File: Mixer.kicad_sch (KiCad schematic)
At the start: 25 parts, among them J39 Noise Out, SW10 SW_SPDT, SW9 SW_SPDT, U11 TL071

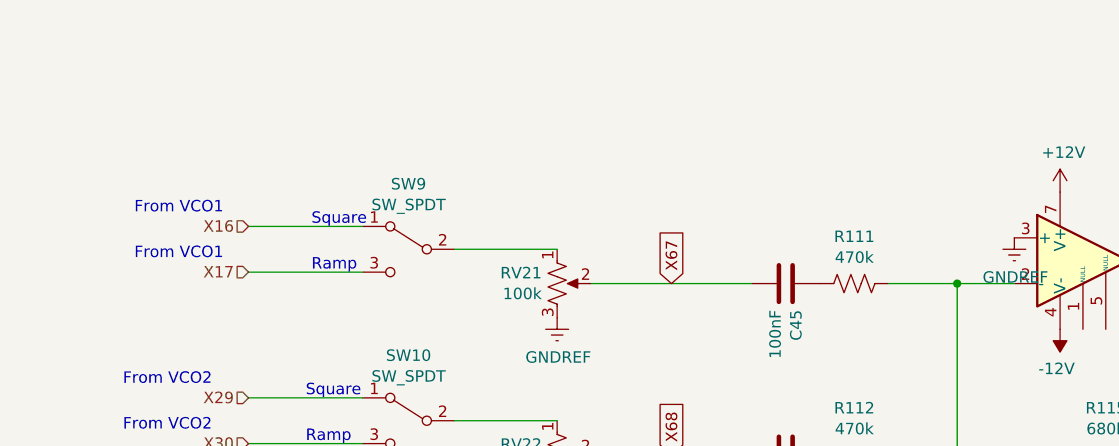
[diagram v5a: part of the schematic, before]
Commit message: lots of routes, added vco3, lfo2.
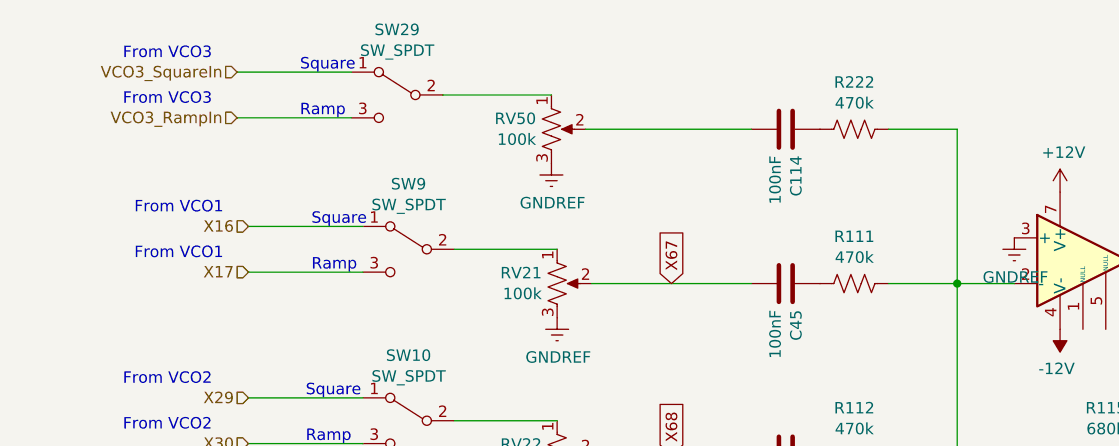
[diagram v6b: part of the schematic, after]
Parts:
- added C114: 100nF, Capacitor_SMD:C_0603_1608Metric, symbol Device:C
- added R222: 470k, Resistor_SMD:R_0603_1608Metric, symbol Device:R_US
- added RV50: 100k, Potentiometer_THT:Potentiometer_Alps_RK09K_Single_Vertical, symbol SynthProj-rescue:R_POT_US-Device
- added SW29: SW_SPDT, SynthProjConnectors:SMTS-102, symbol Switch:SW_SPDT
- J39: footprint SynthProjConnectors:PJ-301 -> SynthProjConnectors:PJ-301-BM
- SW10, SW9: footprint SynthProjConnectors:MTS-103-A01-T0 -> SynthProjConnectors:SMTS-102
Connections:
- net GNDREF: now also RV50.3
- net at R111.1, R112.1, R113.1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: now also R222.1
- new net: RV50.1, SW29.2 (B)
- new net: C114.1, R222.2
- new net: C114.2, RV50.2
- new net VCO3_RampIn: SW29.3 (C)
- new net VCO3_SquareIn: SW29.1 (A)
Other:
- note added: "From VCO3"
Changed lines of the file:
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@@
+    (stroke (width 0) (type default))
+  )
+  (wire (pts (xy 105.41 51.435) (xy 92.71 51.435))
     (stroke (width 0) (type default))
   )
@@
     (stroke (width 0) (type default))
   )
+  (wire (pts (xy 172.72 52.705) (xy 172.72 69.85))
+    (stroke (width 0) (type default))
+  )
   (wire (pts (xy 86.36 148.59) (xy 92.71 148.59))
     (stroke (width 0) (type default))
@@
     (stroke (width 0) (type default))
   )
+  (wire (pts (xy 105.41 46.355) (xy 92.71 46.355))
+    (stroke (width 0) (type default))
+  )
   (wire (pts (xy 132.08 69.85) (xy 149.86 69.85))
     (stroke (width 0) (type default))
@@
     (stroke (width 0) (type default))
   )
+  (wire (pts (xy 131.445 52.705) (xy 149.86 52.705))
+    (stroke (width 0) (type default))
+  )
+  (wire (pts (xy 115.57 48.895) (xy 127.635 48.895))
+    (stroke (width 0) (type default))
+  )
   (wire (pts (xy 201.93 88.9) (xy 201.93 67.31))
     (stroke (width 0) (type default))
@@
     (stroke (width 0) (type default))
   )
+  (wire (pts (xy 165.1 52.705) (xy 172.72 52.705))
+    (stroke (width 0) (type default))
+  )
   (wire (pts (xy 132.08 109.22) (xy 149.86 109.22))
     (stroke (width 0) (type default))
@@
     (effects (font (size 1.27 1.27)) (justify left bottom))
   )
+  (text "From VCO3" (at 80.01 50.165 0)
+    (effects (font (size 1.27 1.27)) (justify left bottom))
+  )
+  (text "Ramp" (at 99.695 51.435 0)
+    (effects (font (size 1.27 1.27)) (justify left bottom))
+  )
+  (text "Square" (at 99.695 46.355 0)
+    (effects (font (size 1.27 1.27)) (justify left bottom))
+  )
   (text "Ramp" (at 100.965 68.58 0)
+    (effects (font (size 1.27 1.27)) (justify left bottom))
+  )
+  (text "From VCO3" (at 80.01 45.085 0)
     (effects (font (size 1.27 1.27)) (justify left bottom))
   )
@@
     (effects (font (size 1.27 1.27)) (justify left))
   )
+  (hierarchical_label "VCO3_SquareIn" (shape input) (at 92.71 46.355 180) (fields_autoplaced)
+    (effects (font (size 1.27 1.27)) (justify right))
+  )
+  (hierarchical_label "VCO3_RampIn" (shape input) (at 92.71 51.435 180) (fields_autoplaced)
+    (effects (font (size 1.27 1.27)) (justify right))
+  )
   (hierarchical_label "X16" (shape input) (at 93.98 63.5 180) (fields_autoplaced)
     (effects (font (size 1.27 1.27)) (justify right))
@@
       (effects (font (size 1.27 1.27)))
     )
-    (property "Footprint" "SynthProjConnectors:MTS-103-A01-T0" (at 111.76 66.04 0)
+    (property "Footprint" "SynthProjConnectors:SMTS-102" (at 111.76 66.04 0)
       (effects (font (size 1.27 1.27)) hide)
     )
@@
       (effects (font (size 1.27 1.27)))
     )
-    (property "Footprint" "SynthProjConnectors:MTS-103-A01-T0" (at 111.76 85.09 0)
+    (property "Footprint" "SynthProjConnectors:SMTS-102" (at 111.76 85.09 0)
       (effects (font (size 1.27 1.27)) hide)
     )
@@
       (effects (font (size 1.27 1.27)))
     )
-    (property "Footprint" "SynthProjConnectors:PJ-301" (at 102.87 99.06 0)
+    (property "Footprint" "SynthProjConnectors:PJ-301-BM" (at 102.87 99.06 0)
       (effects (font (size 1.27 1.27)) hide)
     )
@@
     )
   )
+  (symbol (lib_id "Switch:SW_SPDT") (at 110.49 48.895 0) (mirror y) (unit 1)
+    (in_bom yes) (on_board yes) (dnp no)
+    (property "Reference" "SW29" (at 110.49 41.656 0)
+      (effects (font (size 1.27 1.27)))
+    )
+    (property "Value" "SW_SPDT" (at 110.49 43.9674 0)
+      (effects (font (size 1.27 1.27)))
+    )
+    (property "Footprint" "SynthProjConnectors:SMTS-102" (at 110.49 48.895 0)
+      (effects (font (size 1.27 1.27)) hide)
+    )
+    (property "Datasheet" "~" (at 110.49 48.895 0)
+      (effects (font (size 1.27 1.27)) hide)
+    )
+    (pin "1")
+    (pin "2")
+    (pin "3")
+    (instances
+      (project "SynthProj"
+        (path "/9021c97e-351f-4ed9-b393-50257df6a463/00000000-0000-0000-0000-00006611e0f5"
+          (reference "SW29") (unit 1)
+        )
+      )
+    )
+  )
+  (symbol (lib_id "Device:C") (at 153.67 52.705 270) (unit 1)
+    (in_bom yes) (on_board yes) (dnp no)
+    (property "Reference" "C114" (at 154.8384 55.626 0)
+      (effects (font (size 1.27 1.27)) (justify left))
+    )
+    (property "Value" "100nF" (at 152.527 55.626 0)
+      (effects (font (size 1.27 1.27)) (justify left))
+    )
+    (property "Footprint" "Capacitor_SMD:C_0603_1608Metric" (at 149.86 53.6702 0)
+      (effects (font (size 1.27 1.27)) hide)
+    )
+    (property "Datasheet" "~" (at 153.67 52.705 0)
+      (effects (font (size 1.27 1.27)) hide)
+    )
+    (pin "2")
+    (pin "1")
+    (instances
+      (project "SynthProj"
+        (path "/9021c97e-351f-4ed9-b393-50257df6a463/00000000-0000-0000-0000-00006611e0f5"
+          (reference "C114") (unit 1)
+        )
+        (path "/9021c97e-351f-4ed9-b393-50257df6a463/00000000-0000-0000-0000-0000659a4e2e"
+          (reference "C?") (unit 1)
+        )
+      )
+    )
+  )
+  (symbol (lib_id "SynthProj-rescue:R_POT_US-Device") (at 127.635 52.705 0) (unit 1)
+    (in_bom yes) (on_board yes) (dnp no)
+    (property "Reference" "RV50" (at 125.9332 51.5366 0)
+      (effects (font (size 1.27 1.27)) (justify right))
+    )
+    (property "Value" "100k" (at 125.9332 53.848 0)
+      (effects (font (size 1.27 1.27)) (justify right))
+    )
+    (property "Footprint" "Potentiometer_THT:Potentiometer_Alps_RK09K_Single_Vertical" (at 127.635 52.705 0)
+      (effects (font (size 1.27 1.27)) hide)
+    )
+    (property "Datasheet" "~" (at 127.635 52.705 0)
+      (effects (font (size 1.27 1.27)) hide)
+    )
+    (pin "3")
+    (pin "2")
+    (pin "1")
+    (instances
+      (project "SynthProj"
+        (path "/9021c97e-351f-4ed9-b393-50257df6a463/00000000-0000-0000-0000-00006611e0f5"
+          (reference "RV50") (unit 1)
+        )
+        (path "/9021c97e-351f-4ed9-b393-50257df6a463/00000000-0000-0000-0000-0000659a4e2e"
+          (reference "RV?") (unit 1)
+        )
+        (path "/9021c97e-351f-4ed9-b393-50257df6a463"
+          (reference "RV?") (unit 1)
+        )
+      )
+    )
+  )
   (symbol (lib_id "Device:C") (at 154.305 146.05 270) (unit 1)
     (in_bom yes) (on_board yes) (dnp no)
@@
         )
         (path "/9021c97e-351f-4ed9-b393-50257df6a463/00000000-0000-0000-0000-0000659a4e2e"
+          (reference "R?") (unit 1)
+        )
+      )
+    )
+  )
+  (symbol (lib_id "power:GNDREF") (at 127.635 56.515 0) (unit 1)
+    (in_bom yes) (on_board yes) (dnp no)
+    (property "Reference" "#PWR0255" (at 127.635 62.865 0)
+      (effects (font (size 1.27 1.27)) hide)
+    )
+    (property "Value" "GNDREF" (at 127.762 60.9092 0)
+      (effects (font (size 1.27 1.27)))
+    )
+    (property "Footprint" "" (at 127.635 56.515 0)
+      (effects (font (size 1.27 1.27)) hide)
+    )
+    (property "Datasheet" "" (at 127.635 56.515 0)
+      (effects (font (size 1.27 1.27)) hide)
+    )
+    (pin "1")
+    (instances
+      (project "SynthProj"
+        (path "/9021c97e-351f-4ed9-b393-50257df6a463/00000000-0000-0000-0000-00006611e0f5"
+          (reference "#PWR0255") (unit 1)
+        )
+      )
+    )
+  )
+  (symbol (lib_id "Device:R_US") (at 161.29 52.705 270) (unit 1)
+    (in_bom yes) (on_board yes) (dnp no)
+    (property "Reference" "R222" (at 161.29 47.498 90)
+      (effects (font (size 1.27 1.27)))
+    )
+    (property "Value" "470k" (at 161.29 49.8094 90)
+      (effects (font (size 1.27 1.27)))
+    )
+    (property "Footprint" "Resistor_SMD:R_0603_1608Metric" (at 161.036 53.721 90)
+      (effects (font (size 1.27 1.27)) hide)
+    )
+    (property "Datasheet" "~" (at 161.29 52.705 0)
+      (effects (font (size 1.27 1.27)) hide)
+    )
+    (pin "2")
+    (pin "1")
+    (instances
+      (project "SynthProj"
+        (path "/9021c97e-351f-4ed9-b393-50257df6a463/00000000-0000-0000-0000-00006611e0f5"
+          (reference "R222") (unit 1)
+        )
+        (path "/9021c97e-351f-4ed9-b393-50257df6a463/00000000-0000-0000-0000-0000659a4e2e"

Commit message: more and more and more and more and more routing
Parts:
- removed C39, C40: 4.7uF, Capacitor_SMD:C_0805_2012Metric, symbol Device:C
- removed C43, C44: 47nF, Capacitor_SMD:C_0603_1608Metric, symbol Device:C
- added C115, C116: 1uF, Capacitor_SMD:C_0805_2012Metric, symbol Device:C
- added R244, R245: 10k, Resistor_SMD:R_0603_1608Metric, symbol Device:R_US
- added RV42, RV52: 100k, Potentiometer_THT:Potentiometer_Alps_RK09K_Single_Vertical, symbol SynthProj-rescue:R_POT_US-Device
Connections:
- net GNDREF: now also RV42.3, RV52.3
- net at R111.1, R112.1, R113.1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: now also R244.1, R245.1
- net Mixer_ExtIn renamed Mixer_ExtIn1
- new net: C116.1, R245.2
- new net: C115.1, R244.2
- new net: C115.2, RV42.2
- new net: C116.2, RV52.2
- new net Mixer_ExtIn2: RV42.1
- new net Mixer_ExtIn3: RV52.1
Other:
- moved on the sheet: C41, C42, C93, R176

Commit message: created manufacturing files
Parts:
- R111, R112, R176, R222: value 470k -> 200k
- R114, R244, R245: value 10k -> 200k
- RV21, RV22, RV23, RV24, RV42, RV50, RV52: value 100k -> 50k
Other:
- note added: "Audio taper potentiometers for mixer inputs"
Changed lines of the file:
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@@
+    (effects (font (size 1.27 1.27)) (justify left bottom))
+  )
+  (text "Audio taper potentiometers for mixer inputs" (at 113.665 48.26 0)
     (effects (font (size 1.27 1.27)) (justify left bottom))
   )
@@
       (effects (font (size 1.27 1.27)) (justify right))
     )
-    (property "Value" "100k" (at 126.5682 70.993 0)
+    (property "Value" "50k" (at 126.5682 70.993 0)
       (effects (font (size 1.27 1.27)) (justify right))
     )
@@
       (effects (font (size 1.27 1.27)))
     )
-    (property "Value" "470k" (at 161.29 66.9544 90)
+    (property "Value" "200k" (at 161.29 66.9544 90)
       (effects (font (size 1.27 1.27)))
     )
@@
       (effects (font (size 1.27 1.27)))
     )
-    (property "Value" "470k" (at 161.29 86.0044 90)
+    (property "Value" "200k" (at 161.29 86.0044 90)
       (effects (font (size 1.27 1.27)))
     )
@@
       (effects (font (size 1.27 1.27)))
     )
-    (property "Value" "10k" (at 161.29 125.3744 90)
+    (property "Value" "200k" (at 161.29 125.3744 90)
       (effects (font (size 1.27 1.27)))
     )
@@
       (effects (font (size 1.27 1.27)) (justify right))
     )
-    (property "Value" "100k" (at 126.5682 90.043 0)
+    (property "Value" "50k" (at 126.5682 90.043 0)
       (effects (font (size 1.27 1.27)) (justify right))
     )
@@
       (effects (font (size 1.27 1.27)) (justify right))
     )
-    (property "Value" "100k" (at 126.5682 110.363 0)
+    (property "Value" "50k" (at 126.5682 110.363 0)
       (effects (font (size 1.27 1.27)) (justify right))
     )
@@
       (effects (font (size 1.27 1.27)) (justify right))
     )
-    (property "Value" "100k" (at 126.5682 129.413 0)
+    (property "Value" "50k" (at 126.5682 129.413 0)
       (effects (font (size 1.27 1.27)) (justify right))
     )
@@
       (effects (font (size 1.27 1.27)))
     )
-    (property "Value" "10k" (at 161.29 162.2044 90)
+    (property "Value" "200k" (at 161.29 162.2044 90)
       (effects (font (size 1.27 1.27)))
     )
@@
       (effects (font (size 1.27 1.27)) (justify right))
     )
-    (property "Value" "100k" (at 125.9332 53.848 0)
+    (property "Value" "50k" (at 125.9332 53.848 0)
       (effects (font (size 1.27 1.27)) (justify right))
     )
@@
       (effects (font (size 1.27 1.27)))
     )
-    (property "Value" "470k" (at 160.655 178.0794 90)
+    (property "Value" "200k" (at 160.655 178.0794 90)
       (effects (font (size 1.27 1.27)))
     )
@@
       (effects (font (size 1.27 1.27)))
     )
-    (property "Value" "10k" (at 161.29 144.4244 90)
+    (property "Value" "200k" (at 161.29 144.4244 90)
       (effects (font (size 1.27 1.27)))
     )
@@
       (effects (font (size 1.27 1.27)) (justify right))
     )
-    (property "Value" "100k" (at 126.5682 148.463 0)
+    (property "Value" "50k" (at 126.5682 148.463 0)
       (effects (font (size 1.27 1.27)) (justify right))
     )
@@
       (effects (font (size 1.27 1.27)) (justify right))
     )
-    (property "Value" "100k" (at 126.5682 166.243 0)
+    (property "Value" "50k" (at 126.5682 166.243 0)
       (effects (font (size 1.27 1.27)) (justify right))
     )
@@
       (effects (font (size 1.27 1.27)))
     )
-    (property "Value" "470k" (at 161.29 49.8094 90)
-      (effects (font (size 1.27 1.27)))
-    )
+    (property "Value" "200k" (at 161.29 49.8094 90)
+      (effects (font (size 1.27 1.27)))
+    )
